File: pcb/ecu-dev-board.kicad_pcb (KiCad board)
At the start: 4 copper layers, 99.9 x 99.9 mm, 258 parts, among them IC201 MAX9924UAUB+, IC401 74HC14D-Q100,118, IC601 UCC28910DR, IC701 UCC27624DR, J101 MX23A18NF1, J102 39-30-1020, K501 Relay, Q201 MMBT2222A, Q501 MMBT2222A, Q502 MMBTA55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

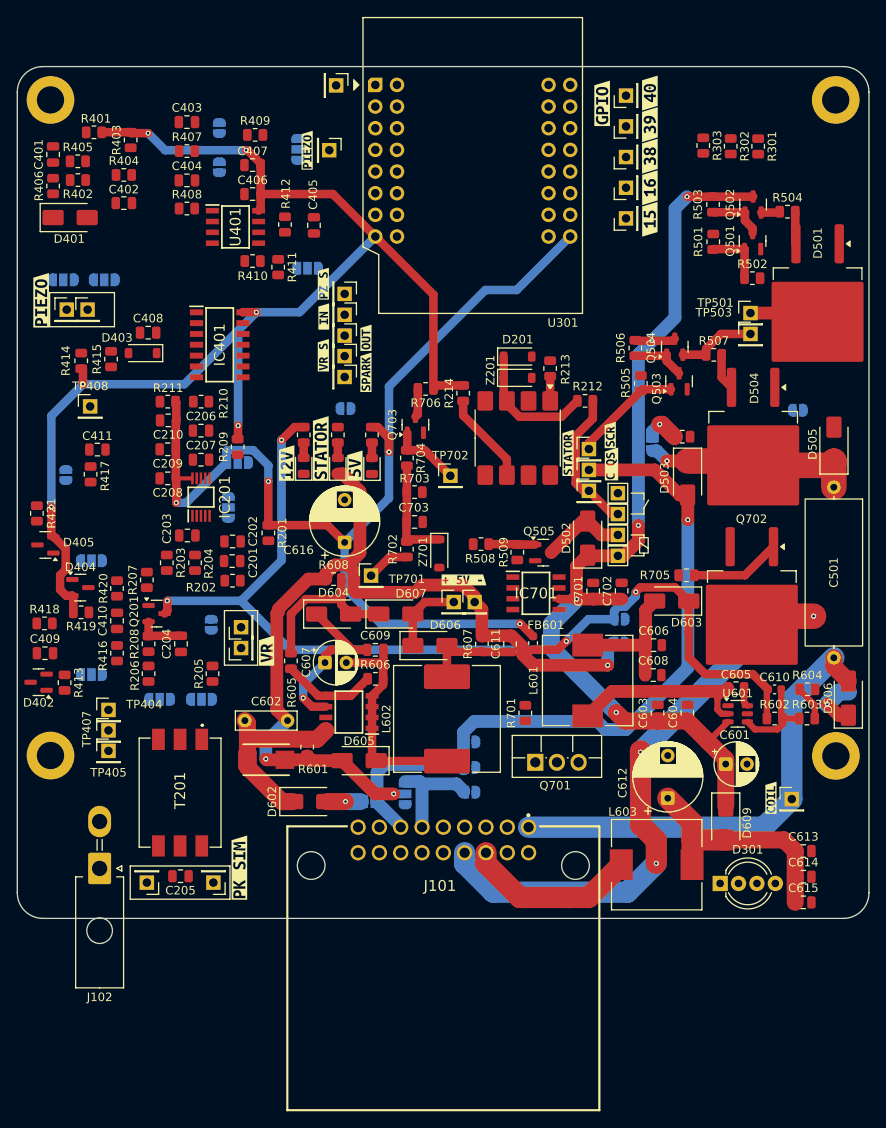
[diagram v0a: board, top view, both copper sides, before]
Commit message: added bigger vias
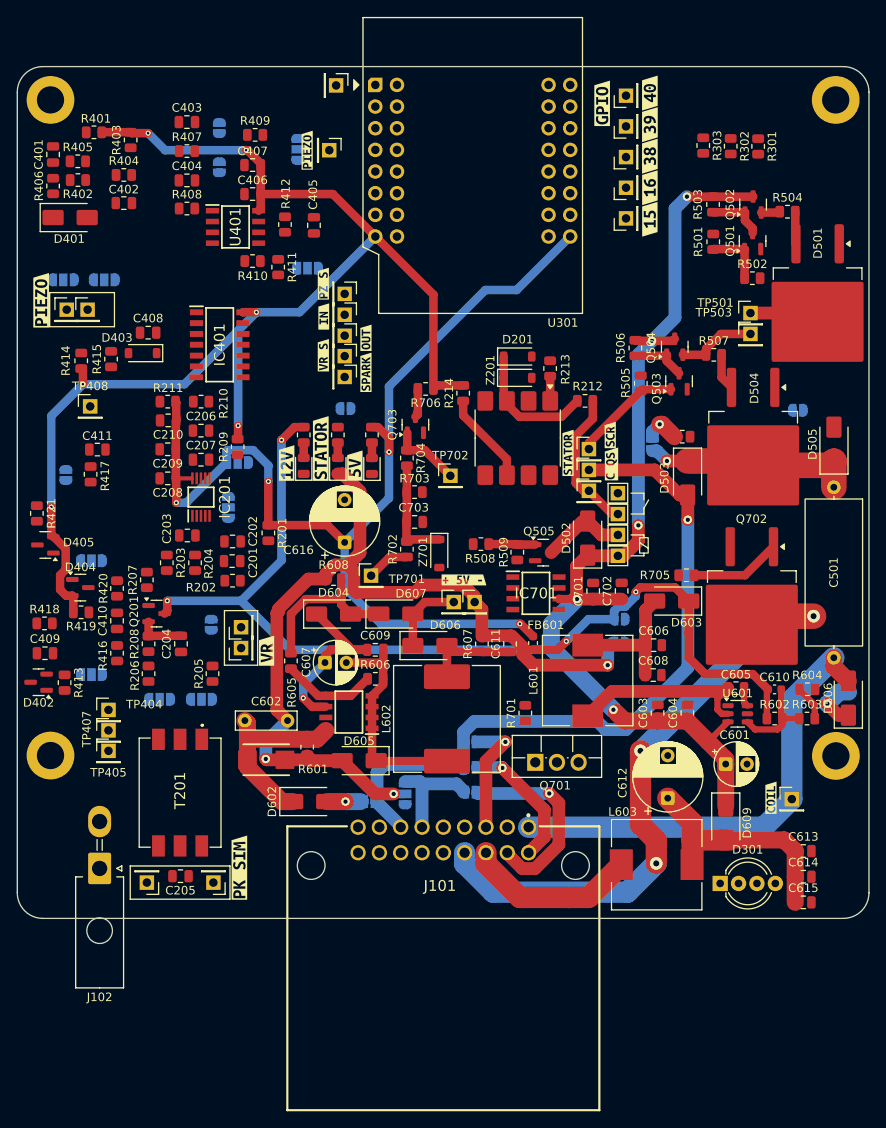
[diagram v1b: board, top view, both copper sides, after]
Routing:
- net VR-: track 0.00 -> 23.0 mm, vias 0 -> 1
- net VR+: track 0.00 -> 15.6 mm, vias 0 -> 1
- net COIL_QS: track 16.9 -> 31.1 mm, vias 0 -> 1
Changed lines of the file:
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@@
+	)
+	(via
+		(at 182.05 117.2)
+		(size 1)
+		(drill 0.5)
+		(layers "F.Cu" "B.Cu")
+		(net 2)
+	)
+	(via
+		(at 197.05 121.3)
+		(size 1)
+		(drill 0.5)
+		(layers "F.Cu" "B.Cu")
+		(net 2)
 	)
 	(via
 		(at 222.15 106.2)
-		(size 0.6)
-		(drill 0.3)
-		(layers "F.Cu" "B.Cu")
-		(net 2)
-	)
-	(via
-		(at 182.05 117.2)
-		(size 0.6)
-		(drill 0.3)
-		(layers "F.Cu" "B.Cu")
-		(net 2)
-	)
-	(via
-		(at 197.05 121.3)
-		(size 0.6)
-		(drill 0.3)
+		(size 1)
+		(drill 0.5)
 		(layers "F.Cu" "B.Cu")
 		(net 2)
@@
 	)
 	(segment
+		(start 218.55 98.45)
+		(end 218.5 98.45)
+		(width 1.5)
+		(layer "F.Cu")
+		(net 17)
+	)
+	(segment
 		(start 234.51 51.2475)
 		(end 239.1925 51.2475)
@@
 	(segment
 		(start 220.45 98.45)
-		(end 218.5 98.45)
-		(width 1.5)
-		(layer "F.Cu")
-		(net 17)
-	)
-	(via
-		(at 218.5 98.45)
-		(size 0.6)
-		(drill 0.3)
-		(layers "F.Cu" "B.Cu")
-		(net 17)
-	)
-	(via
-		(at 223.15 111.75)
-		(size 0.6)
-		(drill 0.3)
+		(end 218.55 98.45)
+		(width 1.5)
+		(layer "F.Cu")
+		(net 17)
+	)
+	(via
+		(at 227.35 68.15)
+		(size 1)
+		(drill 0.5)
+		(layers "F.Cu" "B.Cu")
+		(net 17)
+	)
+	(via
+		(at 225.75 89.8)
+		(size 1)
+		(drill 0.5)
+		(layers "F.Cu" "B.Cu")
+		(net 17)
+	)
+	(via
+		(at 222.825 111.425)
+		(size 1)
+		(drill 0.5)
+		(layers "F.Cu" "B.Cu")
+		(net 17)
+	)
+	(via
+		(at 218.55 98.45)
+		(size 1)
+		(drill 0.5)
 		(layers "F.Cu" "B.Cu")
 		(net 17)
@@
 	)
 	(via
-		(at 225.75 89.8)
-		(size 0.6)
-		(drill 0.3)
-		(layers "F.Cu" "B.Cu")
-		(net 17)
-	)
-	(via
 		(at 170.5 98.65)
 		(size 0.6)
@@
 	)
 	(via
-		(at 227.35 68.15)
-		(size 0.6)
-		(drill 0.3)
-		(layers "F.Cu" "B.Cu")
-		(net 17)
-	)
-	(via
 		(at 231.45 51.25)
-		(size 0.6)
-		(drill 0.3)
+		(size 1)
+		(drill 0.5)
 		(layers "F.Cu" "B.Cu")
 		(net 17)
@@
 	(via
 		(at 231.55 89.15)
-		(size 0.6)
-		(drill 0.3)
+		(size 1)
+		(drill 0.5)
 		(layers "F.Cu" "B.Cu")
 		(net 19)
@@
 	)
 	(via
-		(at 229.1 82.25)
-		(size 0.6)
-		(drill 0.3)
+		(at 229.1025 82.2525)
+		(size 1)
+		(drill 0.5)
 		(layers "F.Cu" "B.Cu")
 		(net 41)
@@
 	)
 	(via
+		(at 226 116.25)
+		(size 1.5)
+		(drill 0.7)
+		(layers "F.Cu" "B.Cu")
+		(net 49)
+	)
+	(via
+		(at 246.3 100.45)
+		(size 1.5)
+		(drill 0.7)
+		(layers "F.Cu" "B.Cu")
+		(net 49)
+	)
+	(via
 		(at 227.85 129.45)
-		(size 0.6)
-		(drill 0.3)
-		(layers "F.Cu" "B.Cu")
-		(net 49)
-	)
-	(via
-		(at 226 116.4)
-		(size 0.6)
-		(drill 0.3)
-		(layers "F.Cu" "B.Cu")
-		(net 49)
-	)
-	(via
-		(at 246.3 100.45)
-		(size 0.6)
-		(drill 0.3)
+		(size 1.5)
+		(drill 0.7)
 		(layers "F.Cu" "B.Cu")
 		(net 49)
@@
 	)
 	(segment
+		(start 212.875 128.2)
+		(end 214.726 126.349)
+		(width 1.5)
+		(layer "F.Cu")
+		(net 52)
+	)
+	(segment
+		(start 214.726 123.176)
+		(end 209.8 118.25)
+		(width 1.5)
+		(layer "F.Cu")
+		(net 52)
+	)
+	(segment
+		(start 214.726 126.349)
+		(end 214.726 123.176)
+		(width 1.5)
+		(layer "F.Cu")
+		(net 52)
+	)
+	(via
+		(at 209.8 118.25)
+		(size 1)
+		(drill 0.5)
+		(layers "F.Cu" "B.Cu")
+		(net 52)
+	)
+	(segment
+		(start 209.75 118.2)
+		(end 206.945 118.2)
+		(width 1.5)
+		(layer "B.Cu")
+		(net 52)
+	)
+	(segment
+		(start 209.8 118.25)
+		(end 209.75 118.2)
+		(width 1.5)
+		(layer "B.Cu")
+		(net 52)
+	)
+	(segment
+		(start 216.427 127.26571)
+		(end 216.427 122.377)
+		(width 1.5)
+		(layer "F.Cu")
+		(net 53)
+	)
+	(segment
+		(start 213.64171 130.051)
+		(end 216.427 127.26571)
+		(width 1.5)
+		(layer "F.Cu")
+		(net 53)
+	)
+	(segment
+		(start 212.10829 130.051)
+		(end 213.64171 130.051)
+		(width 1.5)
+		(layer "F.Cu")
+		(net 53)
+	)
+	(segment
+		(start 216.427 122.377)
+		(end 215.3 121.25)
+		(width 1.5)
+		(layer "F.Cu")
+		(net 53)
+	)
+	(segment
+		(start 210.375 128.2)
+		(end 210.375 128.31771)
+		(width 1.5)
+		(layer "F.Cu")
+		(net 53)
+	)
+	(segment
+		(start 210.375 128.31771)
+		(end 212.10829 130.051)
+		(width 1.5)
+		(layer "F.Cu")
+		(net 53)
+	)
+	(via
+		(at 215.3 121.25)
+		(size 1)
+		(drill 0.5)
+		(layers "F.Cu" "B.Cu")
+		(net 53)
+	)
+	(segment
+		(start 206.945 121.25)
+		(end 206.945 121.1)
+		(width 1.5)
+		(layer "B.Cu")
+		(net 53)
+	)
+	(segment
+		(start 215.3 121.25)
+		(end 206.945 121.25)
+		(width 1.5)
+		(layer "B.Cu")
+		(net 53)
+	)
+	(segment
 		(start 220.4125 75.2)
 		(end 220.4125 77.2855)
@@
 	)
 	(segment
+		(start 207.875 125.2)
+		(end 207.875 117.475)
+		(width 1.5)
+		(layer "F.Cu")
+		(net 57)
+	)
+	(segment
 		(start 220.4125 77.2855)
 		(end 218.399 79.299)
@@
 	)
 	(segment
+		(start 207.875 117.475)
+		(end 210.15 115.2)
+		(width 1.5)
+		(layer "F.Cu")
+		(net 57)
+	)
+	(segment
 		(start 219.298 85.75)
 		(end 219.95 85.75)
@@
 		(width 1)
 		(layer "F.Cu")
+		(net 57)
+	)
+	(via
+		(at 210.15 115.2)
+		(size 1)
+		(drill 0.5)
+		(layers "F.Cu" "B.Cu")
+		(net 57)
+	)
+	(segment
+		(start 210.15 115.2)
+		(end 206.945 115.2)
+		(width 1.5)
+		(layer "B.Cu")
 		(net 57)
 	)
@@
 	)
 	(via
-		(at 247.9 110.75)
-		(size 0.6)
-		(drill 0.3)
+		(at 247.925 110.725)
+		(size 1)
+		(drill 0.5)
 		(layers "F.Cu" "B.Cu")
 		(net 93)
@@
 	(segment
 		(start 247.9 110.75)
+		(end 247.925 110.725)
+		(width 2)
+		(layer "B.Cu")
+		(net 93)
+	)
+	(segment
+		(start 247.925 110.725)
 		(end 249.294 109.356)
 		(width 2)
@@
 	(via
 		(at 191.4 122.2)
-		(size 0.6)
-		(drill 0.3)
+		(size 1)
+		(drill 0.5)
 		(layers "F.Cu" "B.Cu")
 		(net 94)
@@
 	(via
 		(at 228.25 77.95)
-		(size 0.6)
-		(drill 0.3)
+		(size 1)
+		(drill 0.5)
 		(layers "F.Cu" "B.Cu")
 		(net 118)

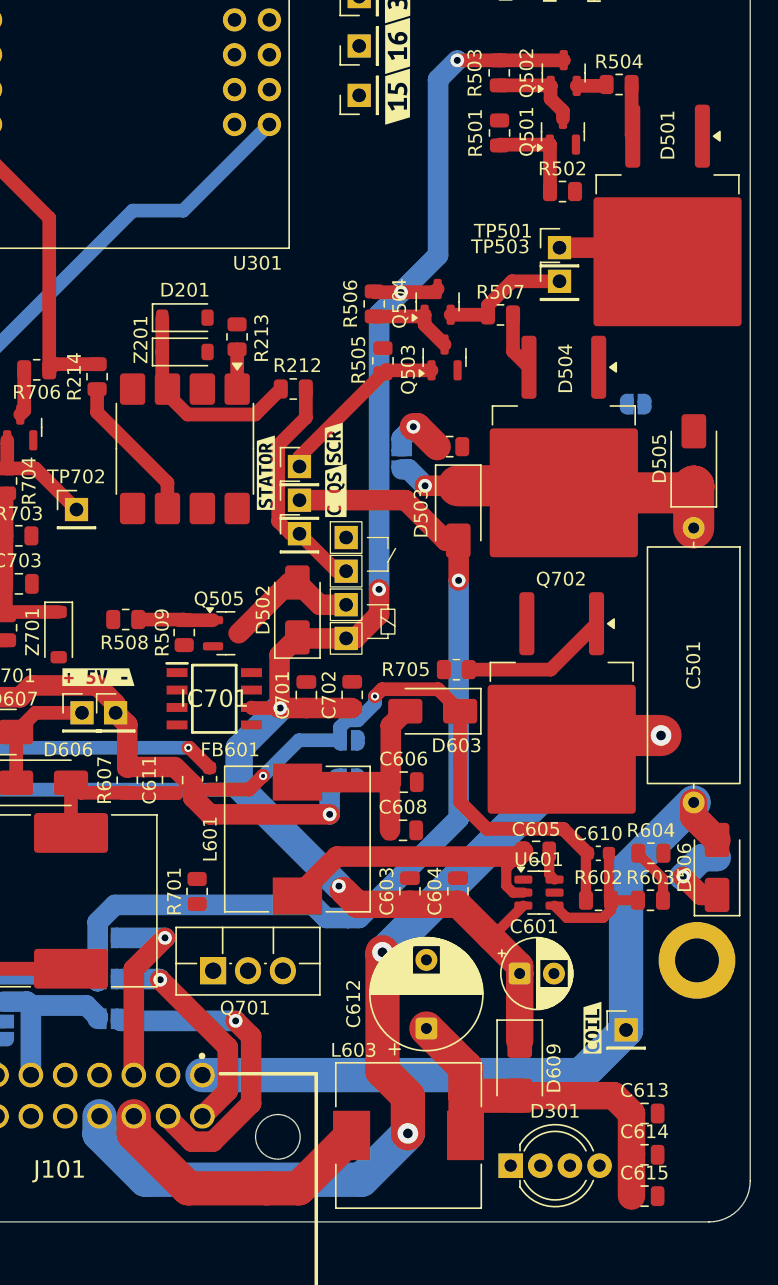
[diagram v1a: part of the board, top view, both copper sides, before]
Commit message: started components grounding using vias
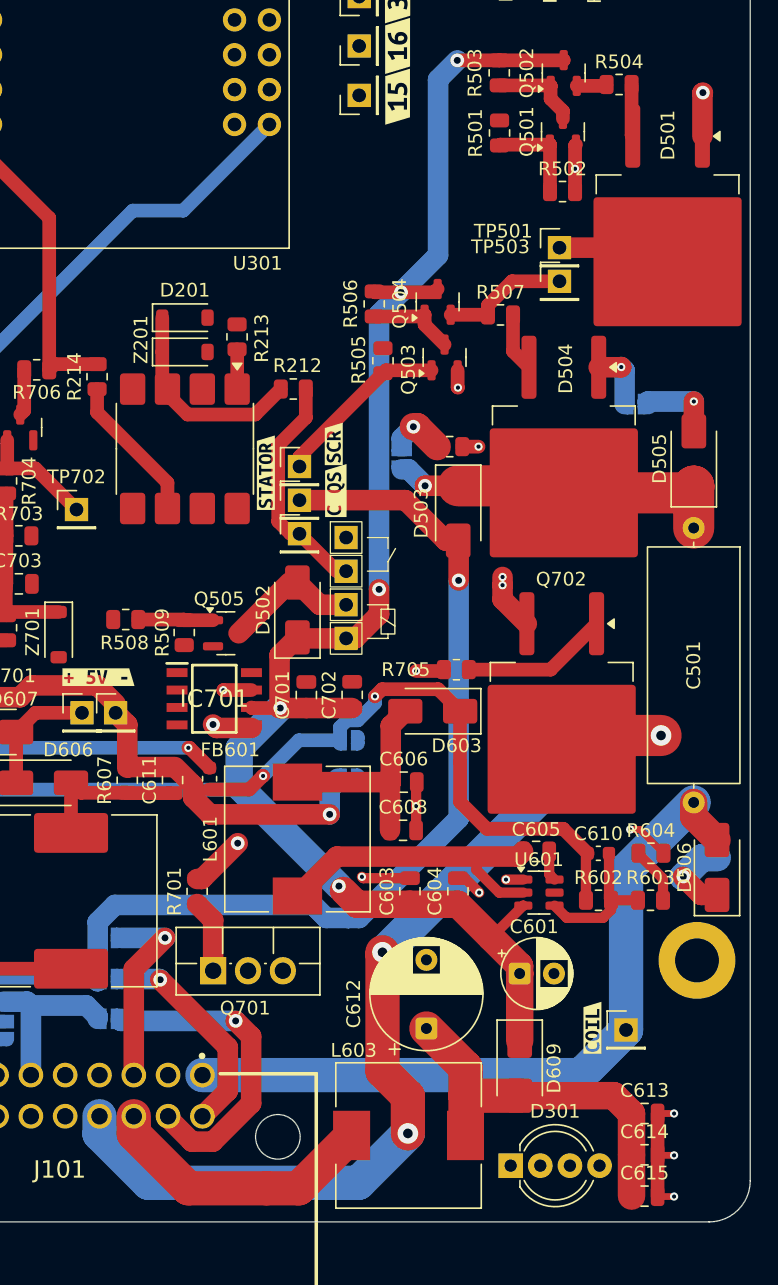
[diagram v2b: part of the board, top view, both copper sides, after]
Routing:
- net GND: track 0.00 -> 40.8 mm, vias 0 -> 15
- net INDUCTIVE: track 0.00 -> 26.9 mm
- net /TCI/IGBT: track 0.00 -> 18.8 mm, vias 0 -> 2
- net /TCI/FET: track 0.00 -> 16.3 mm, vias 0 -> 2
- net Net-(D505-A): track 0.00 -> 5.70 mm, vias 0 -> 1
- net Net-(Q701-G): track 0.00 -> 5.35 mm
- net Net-(U601-SW): track 22.3 -> 22.9 mm
- added copper zone on In1.Cu, net GND

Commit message: completed components grounding using vias
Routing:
- net GND: track 40.8 -> 130.6 mm, vias 15 -> 56

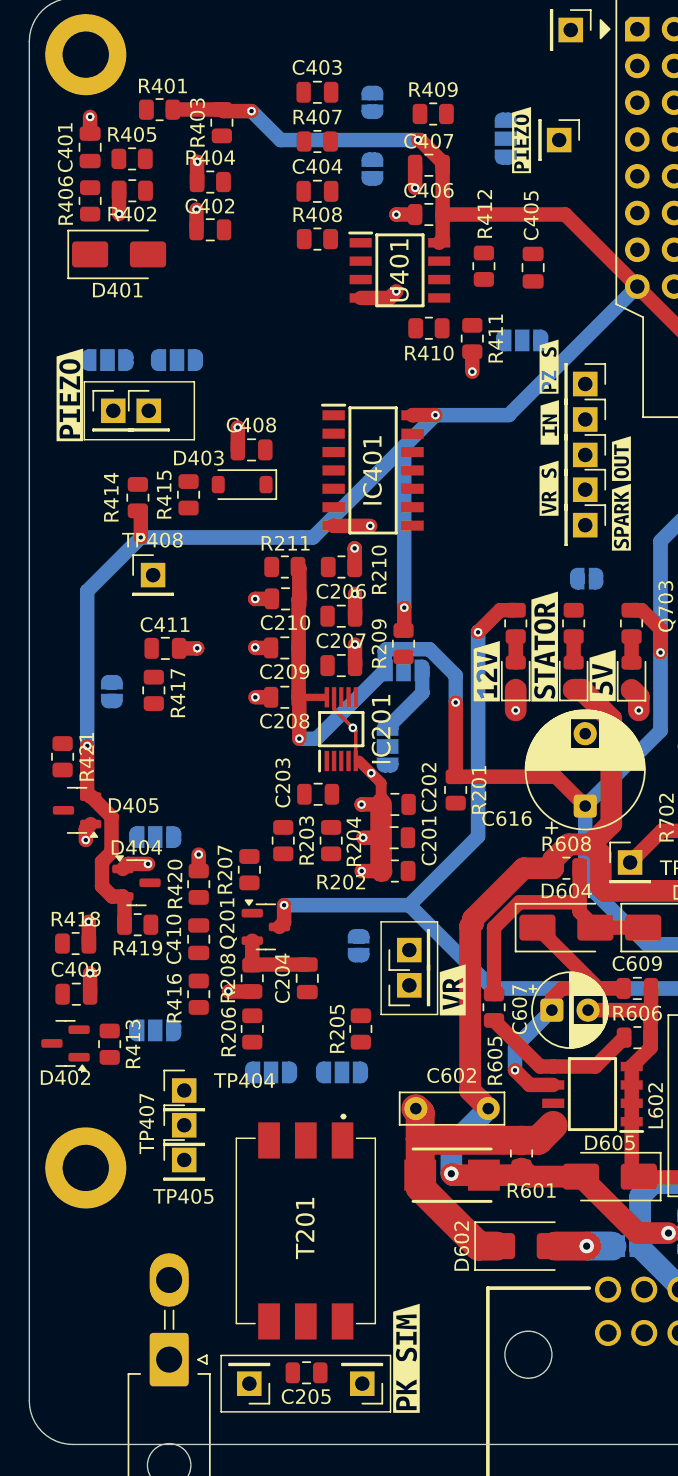
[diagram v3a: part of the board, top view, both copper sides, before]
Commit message: routed OPAMP and Schmitt Trigger
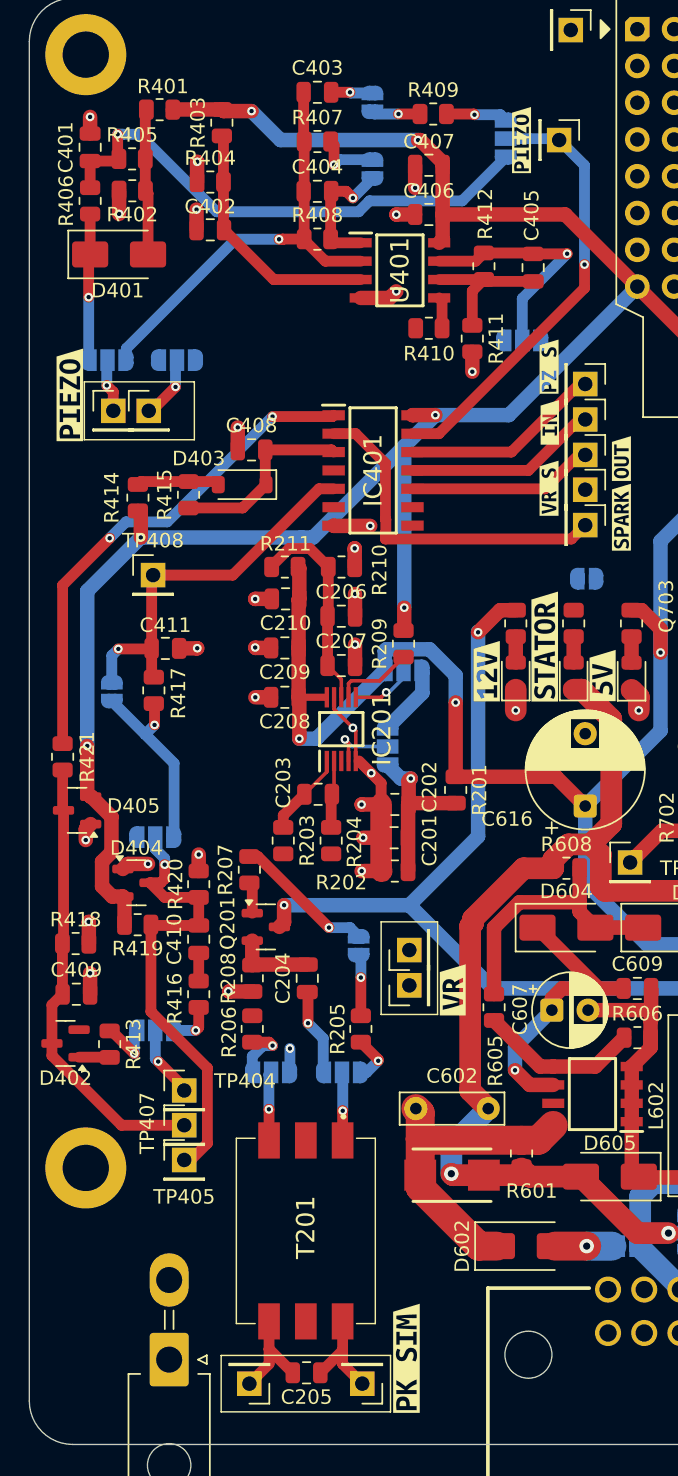
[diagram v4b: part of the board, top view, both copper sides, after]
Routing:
- net /Sensor/PIEZO_BASIC: track 0.00 -> 36.5 mm, vias 0 -> 1
- net /Sensor/ENV_SPARK: track 0.00 -> 34.5 mm, vias 0 -> 2
- net /Sensor/BIAS_CLAMP: track 0.00 -> 32.1 mm, vias 0 -> 1
- net Net-(D402-COM): track 0.00 -> 31.2 mm
- net /Sensor/CHARGE_AMP-: track 0.00 -> 30.9 mm, vias 0 -> 1
- net PIEZO: track 0.00 -> 30.7 mm, vias 0 -> 1
- net /Sensor/COUP_SPARK: track 0.00 -> 26.9 mm, vias 0 -> 1
- net SPARK_TRIGGER: track 0.00 -> 23.9 mm
- net Net-(U401A-+): track 0.00 -> 17.4 mm
- net Net-(JP407-C): track 0.00 -> 16.4 mm, vias 0 -> 1
- net Net-(IC201-EXT): track 0.00 -> 14.4 mm
- net PIEZO_SCHMITT: track 0.00 -> 13.9 mm
- net /Sensor/FILTER: track 0.00 -> 13.6 mm, vias 0 -> 1
- net Net-(IC401-5A): track 0.00 -> 13.4 mm
- net Net-(D403-K): track 0.00 -> 13.2 mm
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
